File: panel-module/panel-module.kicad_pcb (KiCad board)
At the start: 2 copper layers, 40.6 x 30.3 mm, 11 parts, among them J1 East, J2 West, J3 Debug, SW1 Setup, SW2 Reset

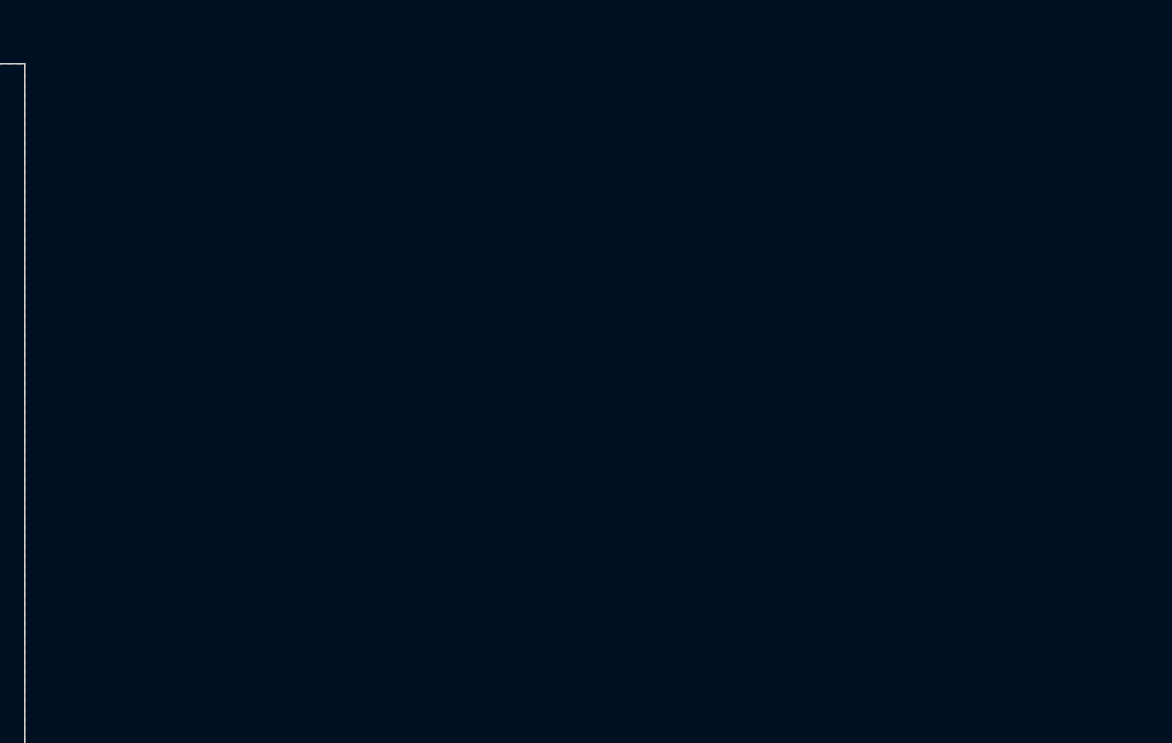
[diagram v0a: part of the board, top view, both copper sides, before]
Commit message: Introduce new serial numbering scheme
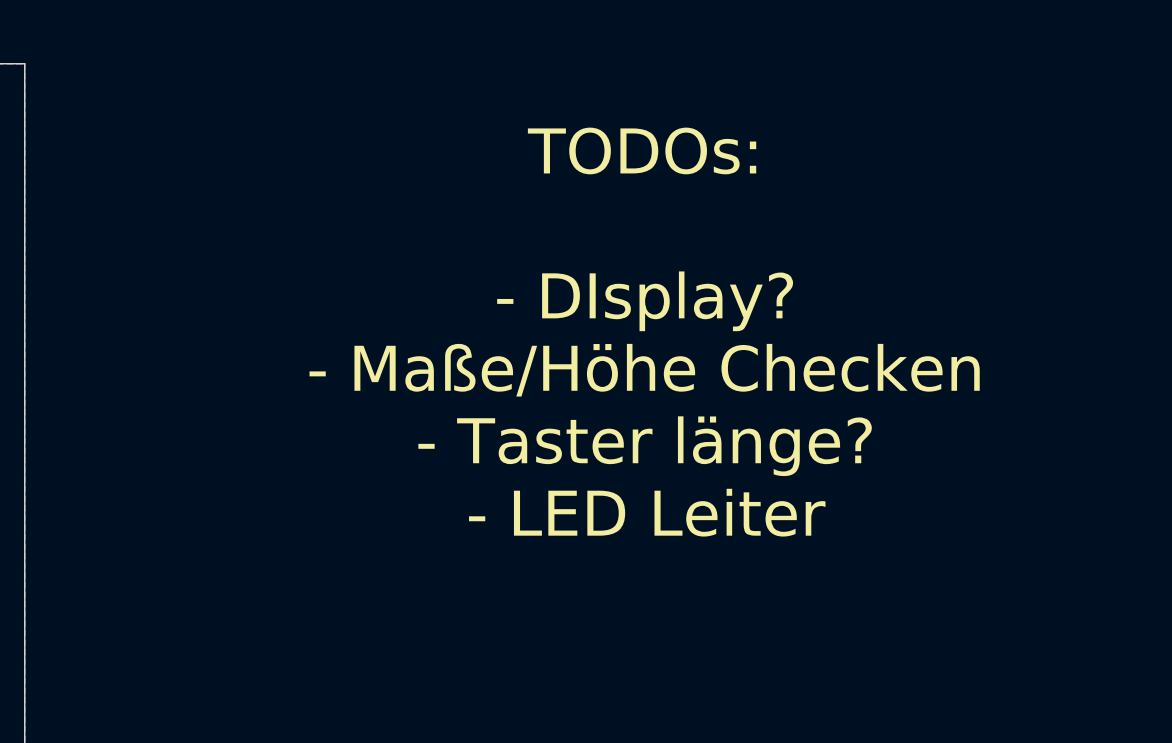
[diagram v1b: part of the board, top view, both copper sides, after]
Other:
- board text added: "TODOs: - DIsplay? - Maße/Höhe Checken - Taster länge? - LED Leiter"
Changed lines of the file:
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@@
   (general
     (thickness 1.6)
-    (drawings 10)
+    (drawings 11)
     (tracks 54)
     (zones 0)
@@
     )
   )
+  (gr_text "TODOs:\n\n- DIsplay?\n- Maße/Höhe Checken\n- Taster länge?\n- LED Leiter" (at 181.3 89) (layer F.SilkS)
+    (effects (font (size 1.5 1.5) (thickness 0.3)))
+  )
   (gr_text TX (at 139.1 92.5 90) (layer F.SilkS)
     (effects (font (size 1 1) (thickness 0.15)))
@@
   (segment (start 149.55 102.35) (end 148 102.35) (width 0.25) (layer F.Cu) (net 22))
   (segment (start 149.8 102.1) (end 149.55 102.35) (width 0.25) (layer F.Cu) (net 22))
-  (via (at 149 105) (size 0.8) (drill 0.4) (layers F.Cu B.Cu) (net 26))
+  (segment (start 143.9375 87.95) (end 144 88.0125) (width 0.25) (layer F.Cu) (net 23))
   (segment (start 143.9375 99.25) (end 144 99.3125) (width 0.25) (layer F.Cu) (net 24))
   (segment (start 147.9375 99.3125) (end 148 99.25) (width 0.25) (layer F.Cu) (net 24))
   (segment (start 144 99.3125) (end 147.9375 99.3125) (width 0.25) (layer F.Cu) (net 24))
-  (segment (start 143.9375 87.95) (end 144 88.0125) (width 0.25) (layer F.Cu) (net 23))
   (segment (start 147.9375 90.9875) (end 148 91.05) (width 0.25) (layer F.Cu) (net 25))
   (segment (start 144 90.9875) (end 147.9375 90.9875) (width 0.25) (layer F.Cu) (net 25))
-  (segment (start 147.9375 88.0125) (end 148 87.95) (width 0.25) (layer F.Cu) (net 27))
+  (via (at 149 105) (size 0.8) (drill 0.4) (layers F.Cu B.Cu) (net 26))
   (segment (start 150.58 85.52) (end 151.75 85.52) (width 0.25) (layer F.Cu) (net 26))
   (segment (start 150.25001 92.4864) (end 150.25001 85.84999) (width 0.25) (layer F.Cu) (net 26))
@@
   (segment (start 147.6 106.4) (end 149 105) (width 0.25) (layer B.Cu) (net 26))
   (segment (start 133.2 106.4) (end 147.6 106.4) (width 0.25) (layer B.Cu) (net 26))
+  (segment (start 147.9375 88.0125) (end 148 87.95) (width 0.25) (layer F.Cu) (net 27))
   (segment (start 123.78 82.2) (end 125.28 83.7) (width 0.25) (layer F.Cu) (net 27))
   (segment (start 125.28 83.7) (end 146.3 83.7) (width 0.25) (layer F.Cu) (net 27))

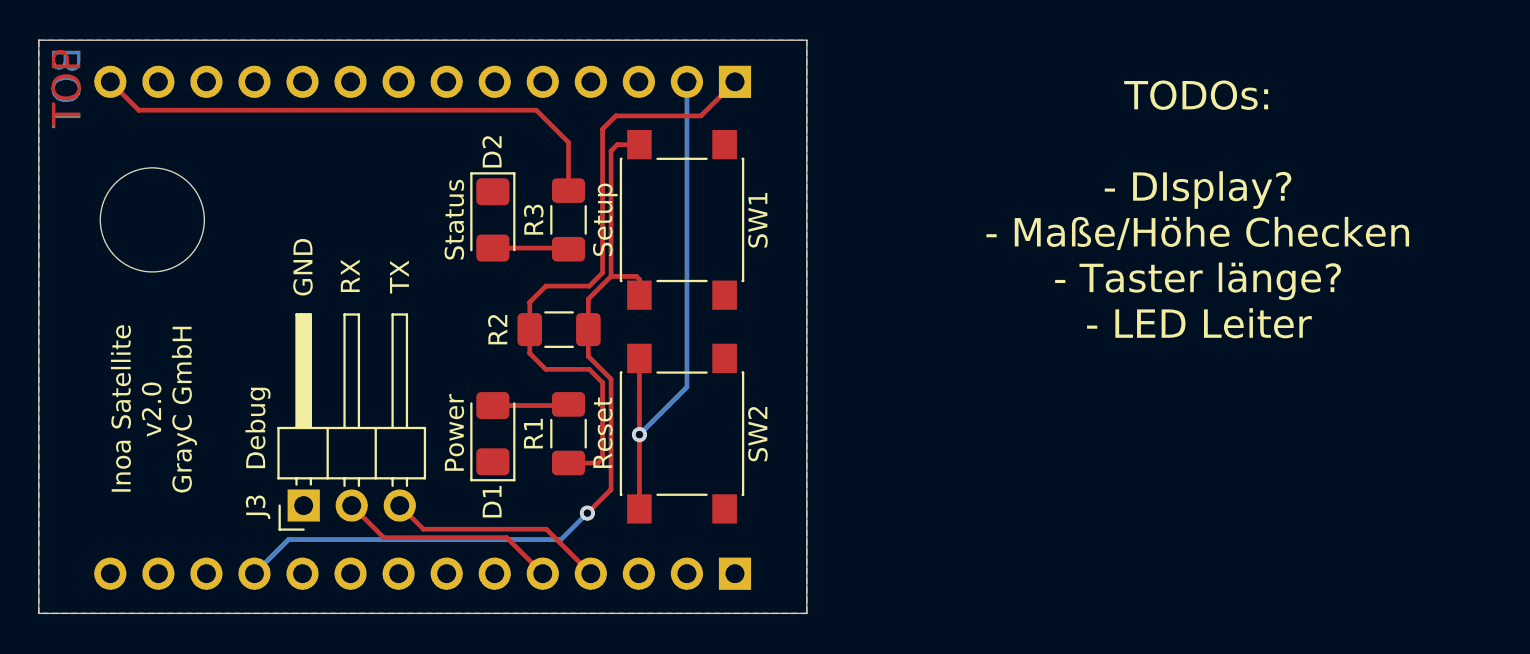
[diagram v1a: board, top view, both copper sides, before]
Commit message: Work on Ethernet module
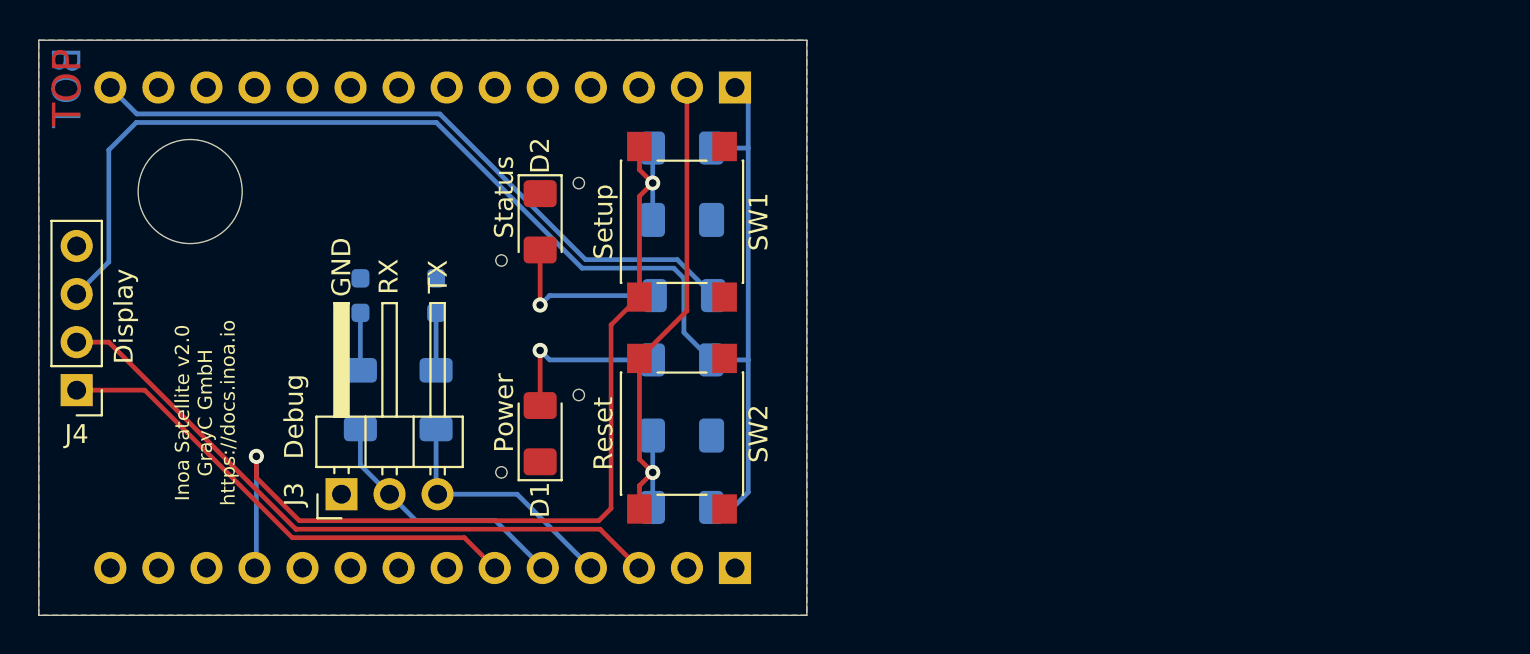
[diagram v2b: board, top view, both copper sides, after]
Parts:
- added C1: 2u2, Capacitor_SMD:C_1206_3216Metric_Pad1.33x1.80mm_HandSolder, B.Cu at (154.0, 100.9)
- added C2: 2u2, Capacitor_SMD:C_1206_3216Metric_Pad1.33x1.80mm_HandSolder, B.Cu at (154.0, 89.5)
- added D3: ESD3.3, Resistor_SMD:R_0603_1608Metric_Pad0.98x0.95mm_HandSolder, B.Cu at (137.0, 93.5)
- added D4: ESD3.3, Resistor_SMD:R_0603_1608Metric_Pad0.98x0.95mm_HandSolder, B.Cu at (141.0, 93.5)
- added G1: LOGO, images:grayc-logo-negative, F.Cu at (123.5, 103.0)
- added J4: Display, Connector_PinHeader_2.54mm:PinHeader_1x04_P2.54mm_Vertical, F.Cu at (122.0, 98.5)
- added R4: 220R, Resistor_SMD:R_1206_3216Metric_Pad1.30x1.75mm_HandSolder, B.Cu at (137.0, 99.0)
- added R5: 220R, Resistor_SMD:R_1206_3216Metric_Pad1.30x1.75mm_HandSolder, B.Cu at (141.0, 99.0)
- added R6: 10k, Resistor_SMD:R_1206_3216Metric_Pad1.30x1.75mm_HandSolder, B.Cu at (154.0, 104.7)
- D1, D2: footprint LED_SMD:LED_1206_3216Metric_Pad1.42x1.75mm_HandSolder -> footprints:LED_1206_3216Metric_Pad1.42x1.75mm_HandSolder_With_Cover
- H1: value WiFi -> Antenna; footprint MountingHole:MountingHole_5.5mm -> footprints:MountingHole_5.5mm_No_Bound
- R1, R2, R3: moved to B.Cu
- moved R2 11.6 mm to (154.0, 85.7), turned to 180 degrees
- moved R3 7.29 mm to (154.1, 93.5), turned to 180 degrees
- moved R1 7.16 mm to (154.0, 96.9), turned to 180 degrees
- moved D2 2.50 mm to (146.5, 89.6)
- moved D1 2.50 mm to (146.5, 100.8)
- moved H1 2.50 mm to (128.0, 88.0)
- moved J3 2.09 mm to (136.0, 104.0)
- moved J1 0.30 mm to (156.8, 107.9)
- moved J2 0.30 mm to (156.8, 82.5)
- moved SW1 0.10 mm to (154.0, 89.6)
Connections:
- J1 pad 3: Net-(J1-Pad3) -> I2C_SCL
- J1 pad 6: Net-(J1-Pad6) -> I2C_SDA
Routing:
- net +3V3: track 33.2 -> 75.5 mm
- net I2C_SCL: track 0.00 -> 34.7 mm
- net I2C_SDA: track 0.00 -> 26.0 mm
- net Panel_Status: track 28.2 -> 36.4 mm
- net Panel_Setup: track 43.6 -> 51.2 mm, vias 1 -> 2
- net Net-(D2-Pad2): track 4.03 -> 9.17 mm, vias 0 -> 1
- net Net-(D1-Pad2): track 4.11 -> 9.07 mm, vias 0 -> 1
- net Net-(D4-Pad1): track 0.00 -> 3.04 mm
- net Net-(D3-Pad1): track 0.00 -> 3.04 mm
- net U0RXD: track 11.6 -> 13.8 mm
- net U0TXD: track 11.6 -> 13.2 mm
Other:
- board size 40.6 x 30.3 mm -> 40.6 x 30.4 mm
- board text added: "Inoa Satellite v2.0 GrayC GmbH https://docs.inoa.io"
- board text removed: "Inoa Satellite v2.0 GrayC GmbH"
- board text removed: "TODOs: - DIsplay? - Maße/Höhe Checken - Taster länge? - LED Leiter"
